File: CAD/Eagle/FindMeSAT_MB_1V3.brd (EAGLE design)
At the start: 99 x 49.2 mm, 135 parts, among them Q101 ABS07-32.768KHZ, Q651 ABM3B-16MHZ-10-R50-1-U, U1001 CFPT-141-20MHZ, U101 ATXMEGA256A3BU-AU, U1011 OPA354, U1021 OPA354, U1111 LM2831YMF, U1121 LM4120IM5-3.0, U201 SIM808, U301 MPU-9250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

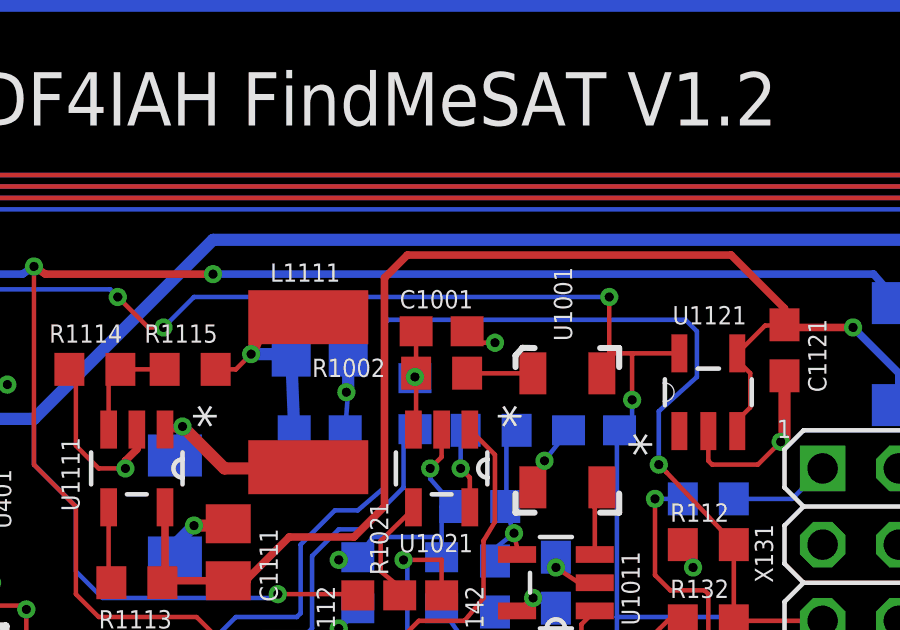
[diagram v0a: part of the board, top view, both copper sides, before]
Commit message: HW_V1.3 - C1001: PWM 100nF changed to 10uF with SMD0805 footprint
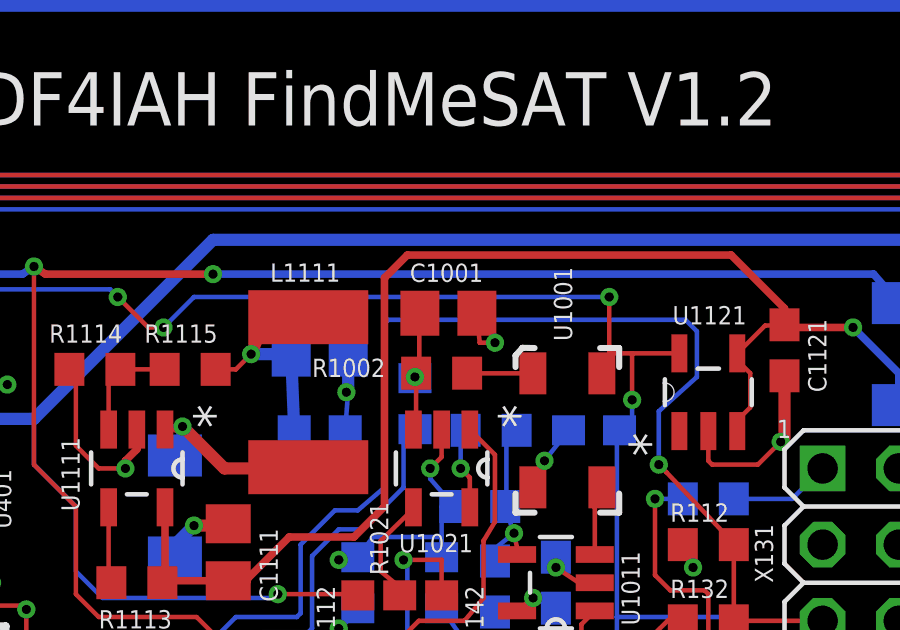
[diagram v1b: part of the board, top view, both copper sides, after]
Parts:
- C1001: device rcl:C0603 -> rcl:C0805
- moved C1001 0.64 mm to (66.3, 36.9)
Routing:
- net XO_LP: track 3.79 -> 4.42 mm
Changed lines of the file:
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@@
 <attribute name="VALUE" x="71.755" y="31.115" size="1.27" layer="28" rot="MR0"/>
 </element>
-<element name="C1001" library="rcl" package="C0603" value="10uF" x="66.04" y="36.322" smashed="yes">
-<attribute name="NAME" x="64.643" y="37.084" size="0.6096" layer="25"/>
-<attribute name="VALUE" x="65.278" y="35.941" size="0.6096" layer="27"/>
+<element name="C1001" library="rcl" package="C0805" value="10uF" x="66.265290625" y="36.922809375" smashed="yes">
+<attribute name="NAME" x="64.980934375" y="37.966440625" size="0.6096" layer="25"/>
+<attribute name="VALUE" x="65.503290625" y="36.541809375" size="0.6096" layer="27"/>
 </element>
 <element name="R1001" library="rcl" package="R0603" value="100kR" x="65.151" y="33.909" smashed="yes" rot="MR90">
@@
 <wire x1="70.27" y1="33.02" x2="69.469" y2="32.004" width="0.1524" layer="16"/>
 <via x="67.818" y="35.941" extent="1-16" drill="0.3048" shape="octagon"/>
-<wire x1="66.89" y1="36.322" x2="67.31" y2="35.941" width="0.1524" layer="1"/>
+<wire x1="67.215290625" y1="36.922809375" x2="67.31" y2="35.941" width="0.1524" layer="1"/>
 <wire x1="67.31" y1="35.941" x2="67.818" y2="35.941" width="0.1524" layer="1"/>
 <wire x1="66.46" y1="30.48" x2="66.04" y2="30.48" width="0.1524" layer="16"/>
@@
 <contactref element="R1002" pad="1"/>
 <contactref element="U1021" pad="3"/>
-<wire x1="65.19" y1="34.925" x2="65.19" y2="36.322" width="0.1524" layer="1"/>
+<wire x1="65.19" y1="34.925" x2="65.296075" y2="35.241196875" width="0.1524" layer="1"/>
+<wire x1="65.296075" y1="35.241196875" x2="65.296075" y2="36.922809375" width="0.1524" layer="1"/>
+<wire x1="65.296075" y1="36.922809375" x2="65.315290625" y2="36.922809375" width="0.1524" layer="1"/>
 <wire x1="65.19" y1="34.925" x2="65.19" y2="33.1352" width="0.1524" layer="1"/>
 <wire x1="65.19" y1="33.1352" x2="65.1002" y2="33.0454" width="0.1524" layer="1"/>

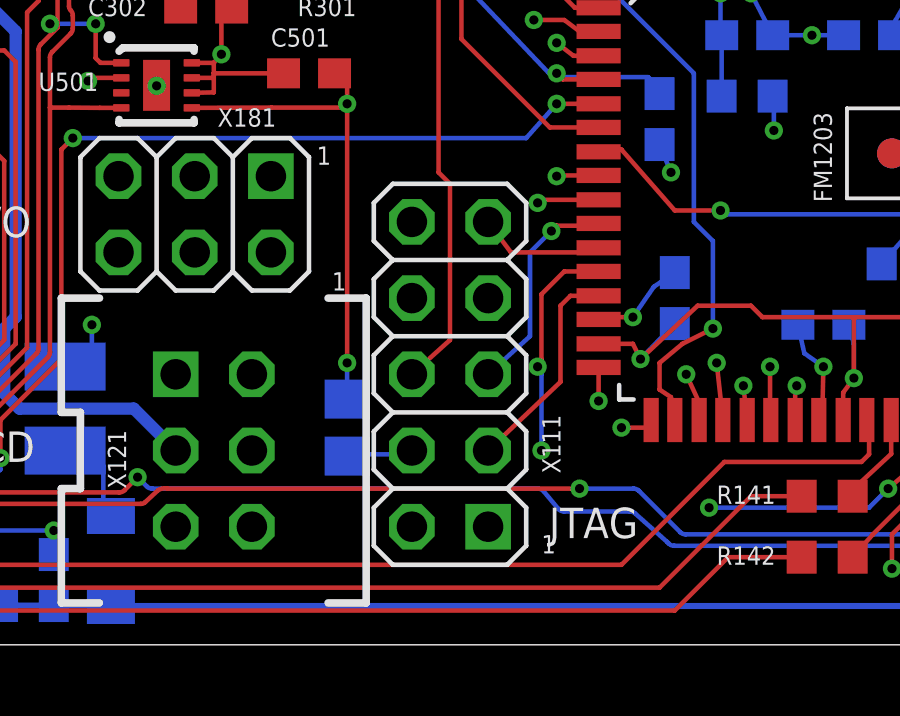
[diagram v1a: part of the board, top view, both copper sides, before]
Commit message: HW_V1.3 - df4iah_connector.lbr combined for Smart-LCD and FindMeSAT (2)
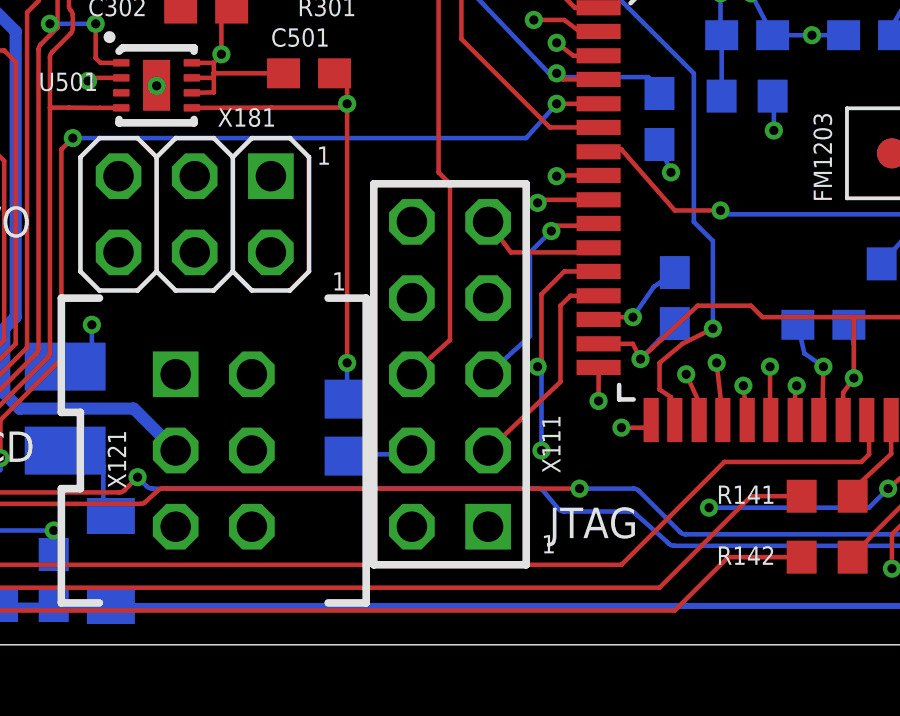
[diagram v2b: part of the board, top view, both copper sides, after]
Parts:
- X111: device df4iah_connector:2X05 -> df4iah_connector:AVR-JTAG-10
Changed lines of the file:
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@@
 <setting verticaltext="up"/>
 </settings>
-<grid distance="1.27" unitdist="mm" unit="mm" style="lines" multiple="1" display="yes" altdistance="0.003125" altunitdist="mic" altunit="mm"/>
+<grid distance="1.27" unitdist="mm" unit="mm" style="lines" multiple="1" display="yes" altdistance="0.127" altunitdist="mm" altunit="mm"/>
 <layers>
 <layer number="1" name="Top" color="4" fill="1" visible="yes" active="yes"/>
@@
 <layer number="37" name="tTest" color="7" fill="1" visible="no" active="yes"/>
 <layer number="38" name="bTest" color="7" fill="1" visible="no" active="yes"/>
-<layer number="39" name="tKeepout" color="4" fill="11" visible="no" active="yes"/>
-<layer number="40" name="bKeepout" color="1" fill="11" visible="no" active="yes"/>
-<layer number="41" name="tRestrict" color="4" fill="10" visible="no" active="yes"/>
-<layer number="42" name="bRestrict" color="1" fill="10" visible="no" active="yes"/>
-<layer number="43" name="vRestrict" color="2" fill="10" visible="no" active="yes"/>
+<layer number="39" name="tKeepout" color="4" fill="11" visible="yes" active="yes"/>
+<layer number="40" name="bKeepout" color="1" fill="11" visible="yes" active="yes"/>
+<layer number="41" name="tRestrict" color="4" fill="10" visible="yes" active="yes"/>
+<layer number="42" name="bRestrict" color="1" fill="10" visible="yes" active="yes"/>
+<layer number="43" name="vRestrict" color="2" fill="10" visible="yes" active="yes"/>
 <layer number="44" name="Drills" color="7" fill="1" visible="yes" active="yes"/>
 <layer number="45" name="Holes" color="7" fill="1" visible="yes" active="yes"/>
@@
 <attribute name="VALUE" x="65.786" y="34.544" size="0.6096" layer="27"/>
 </element>
-<element name="X111" library="df4iah_connector" package="2X05" value="AVR-JTAG-10" x="58.42" y="9.017" smashed="yes" rot="R90">
+<element name="X111" library="df4iah_connector" package="AVR-JTAG-10" value="AVR-JTAG-10" x="58.42" y="9.017" smashed="yes" rot="R90">
 <attribute name="NAME" x="62.103" y="5.715" size="0.6096" layer="25" ratio="10" rot="R90"/>
 <attribute name="VALUE" x="62.357" y="7.747" size="0.8128" layer="27" ratio="20" rot="R90"/>

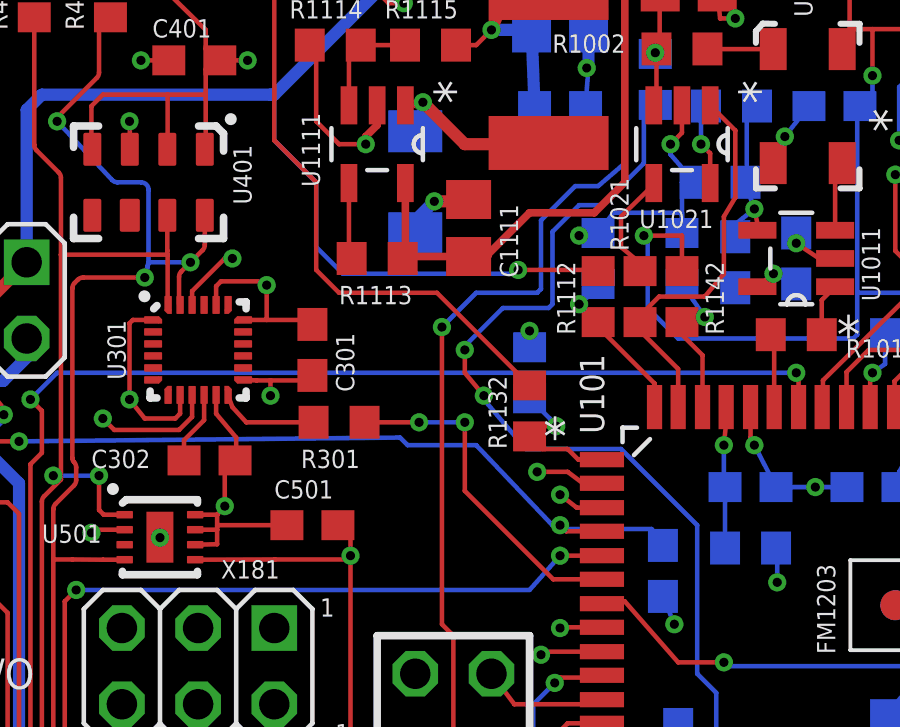
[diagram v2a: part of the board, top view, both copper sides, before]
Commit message: HW_V1.3 - U501 Hygro SHT31-DIS - nRESET to be disconnected, especially from GND
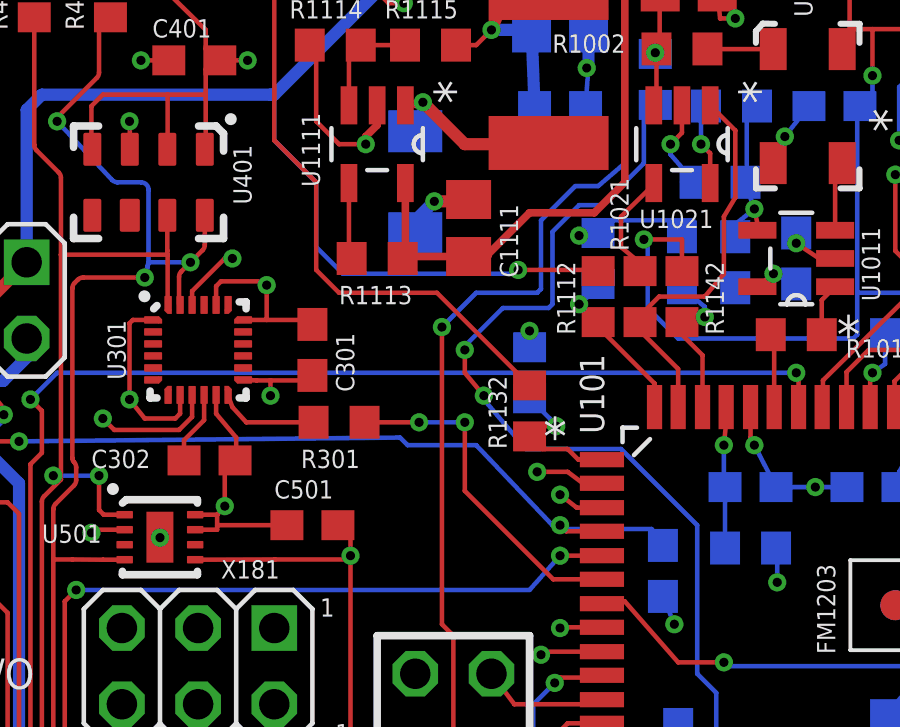
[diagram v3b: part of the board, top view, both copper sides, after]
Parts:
- removed R1141: 4.02kR, rcl:R0603
- added C1141: 100pF, rcl:C0603
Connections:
- removed net AD_3V0: R1141.2, R1142.1, U101.62
- new net AREFA: C1141.1, R1142.1, U101.62
- net GND: now also C1141.2; no longer R1141.1, U501.6
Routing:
- net AD_3V0: track 5.28 -> 0.00 mm, vias 1 -> 0
- net AREFA: track 0.00 -> 5.27 mm, vias 0 -> 1
- net GND: track 233.5 -> 230.1 mm
